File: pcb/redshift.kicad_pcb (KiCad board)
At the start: 4 copper layers, 45 x 63.5 mm, 81 parts, among them IC1 LPC5526JEV98, J1 USB_C_Receptacle_USB2.0, J2 Side, J3 Conn_01x06_Female, J4 Conn_ARM_JTAG_SWD_10, SW1 SW_SP, SW2 SW_SP, SW3 SW_SP, SW4 PTS645, U1 PAW3399DM‐T4QU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

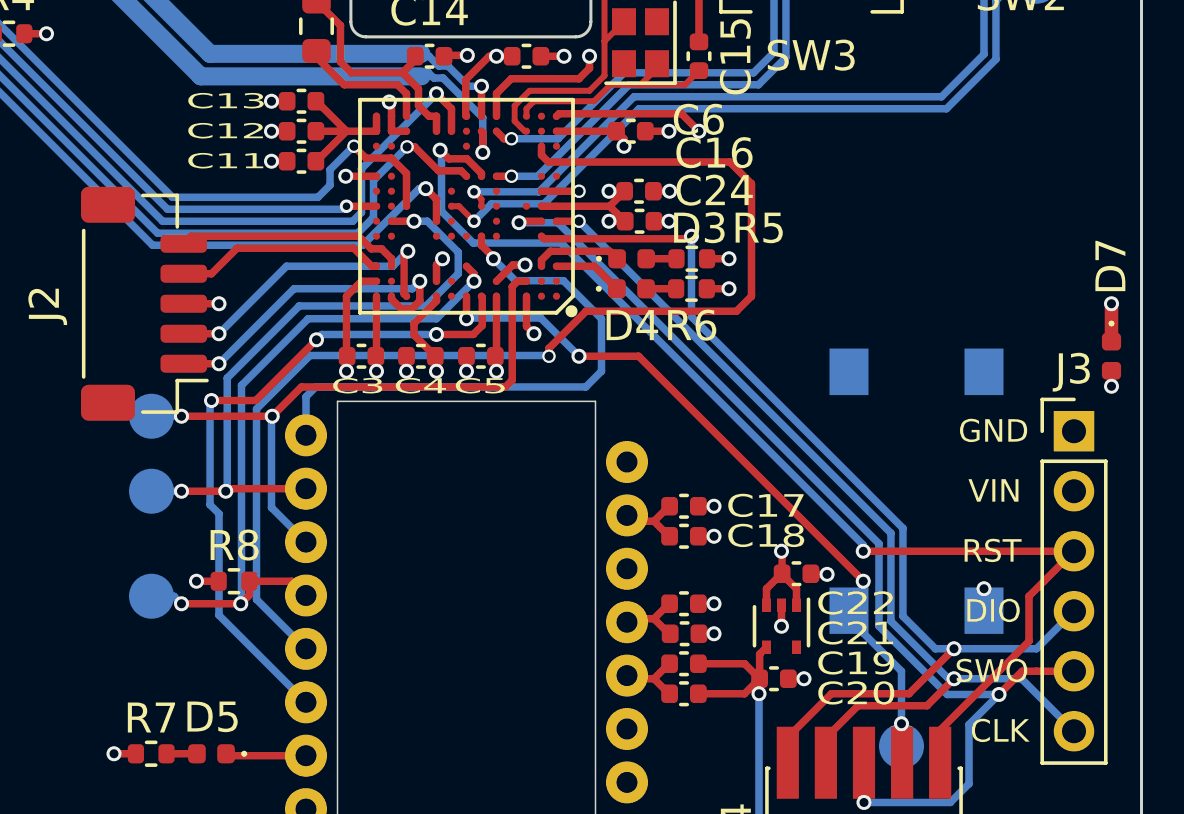
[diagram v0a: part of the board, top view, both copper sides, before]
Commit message: ground unused USB line per datasheet, use smaller switch for ISP
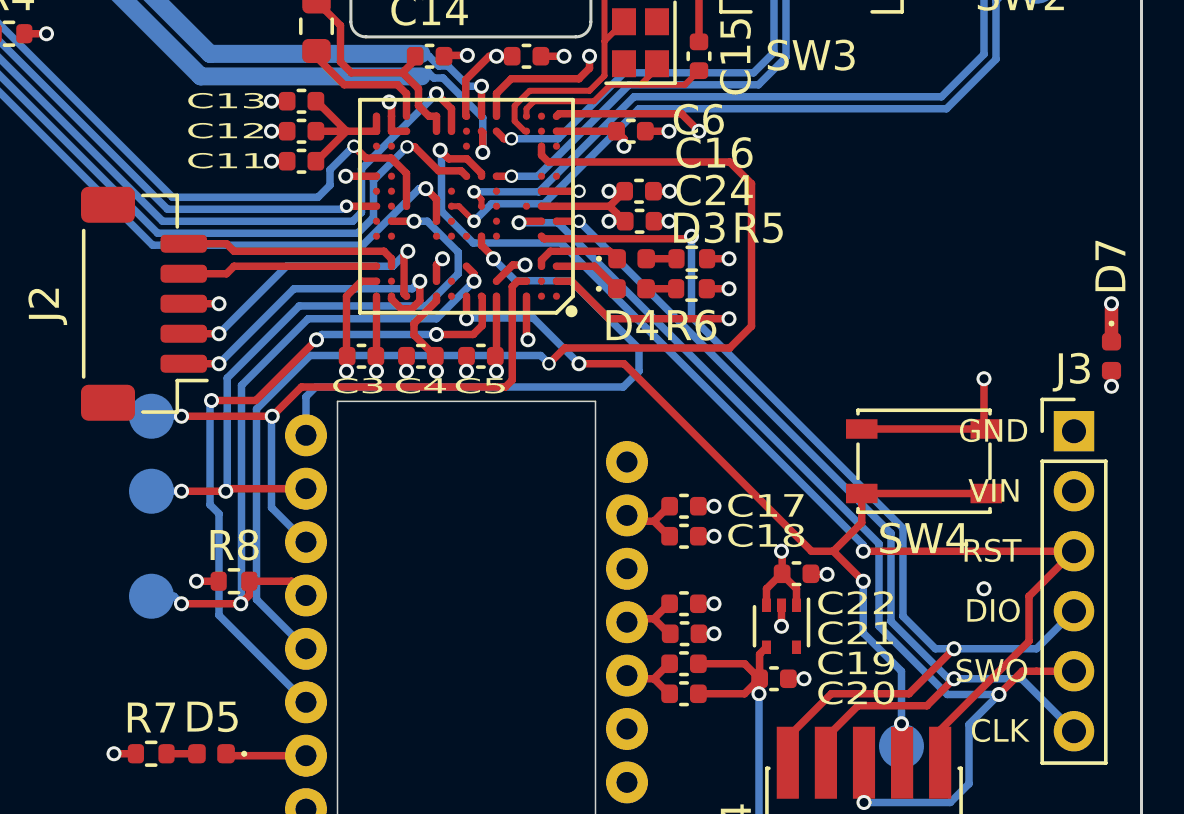
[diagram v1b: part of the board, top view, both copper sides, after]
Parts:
- C11, C14: value 10uF -> 22uF
- C2, C7: value 0.1uF -> 100nF
- SW4: value PTS645 -> PTS810; footprint Button_Switch_SMD:SW_SPST_PTS645 -> Button_Switch_SMD:SW_SPST_PTS810; moved to F.Cu
- moved SW4 1.03 mm to (152.8, 101.5), turned to 180 degrees
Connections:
- IC1 pad B1: unconnected-(IC1-PadB1) -> GND
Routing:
- net GND: track 46.9 -> 59.0 mm, vias 38 -> 40
- net /ISP: track 22.9 -> 29.4 mm
- net /SNSR_MTN: track 18.6 -> 20.5 mm
- net /FC6_CS1: track 38.4 -> 39.0 mm

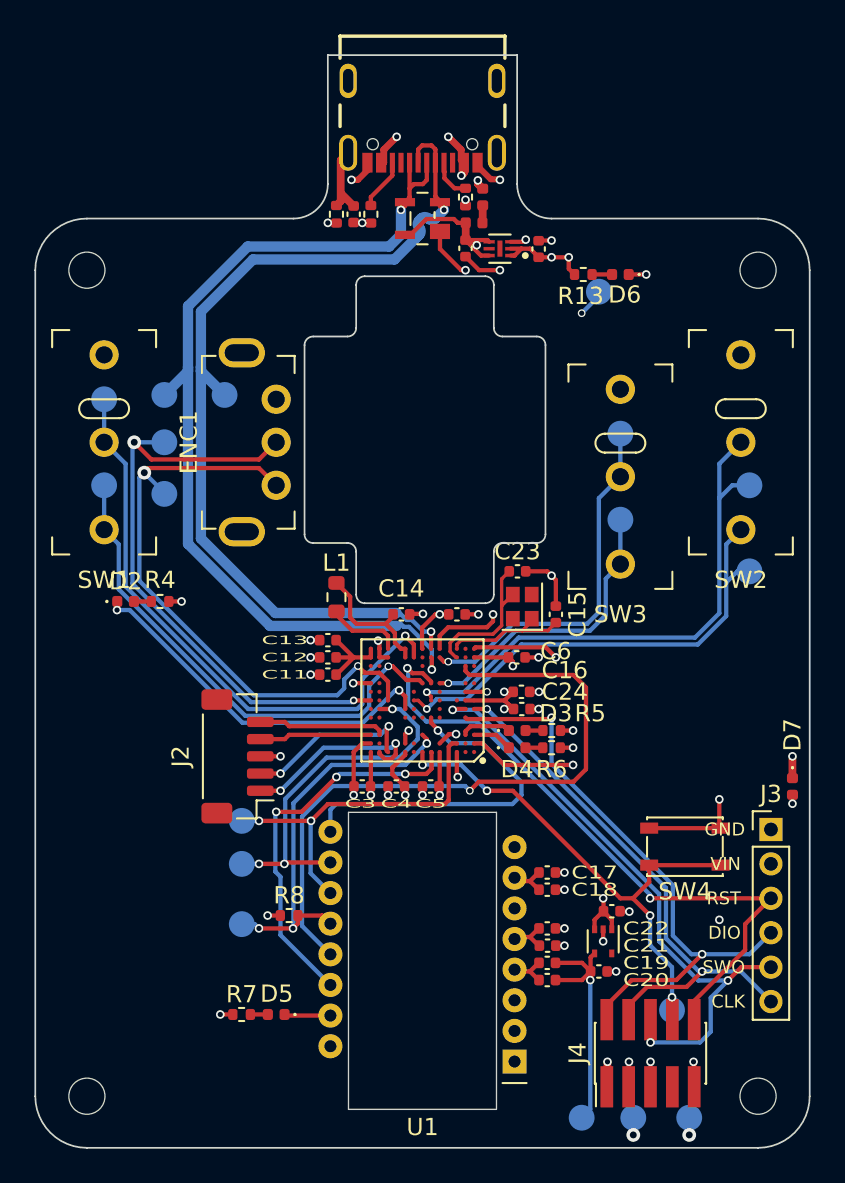
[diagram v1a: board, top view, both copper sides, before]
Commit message: Replaced Old LDO
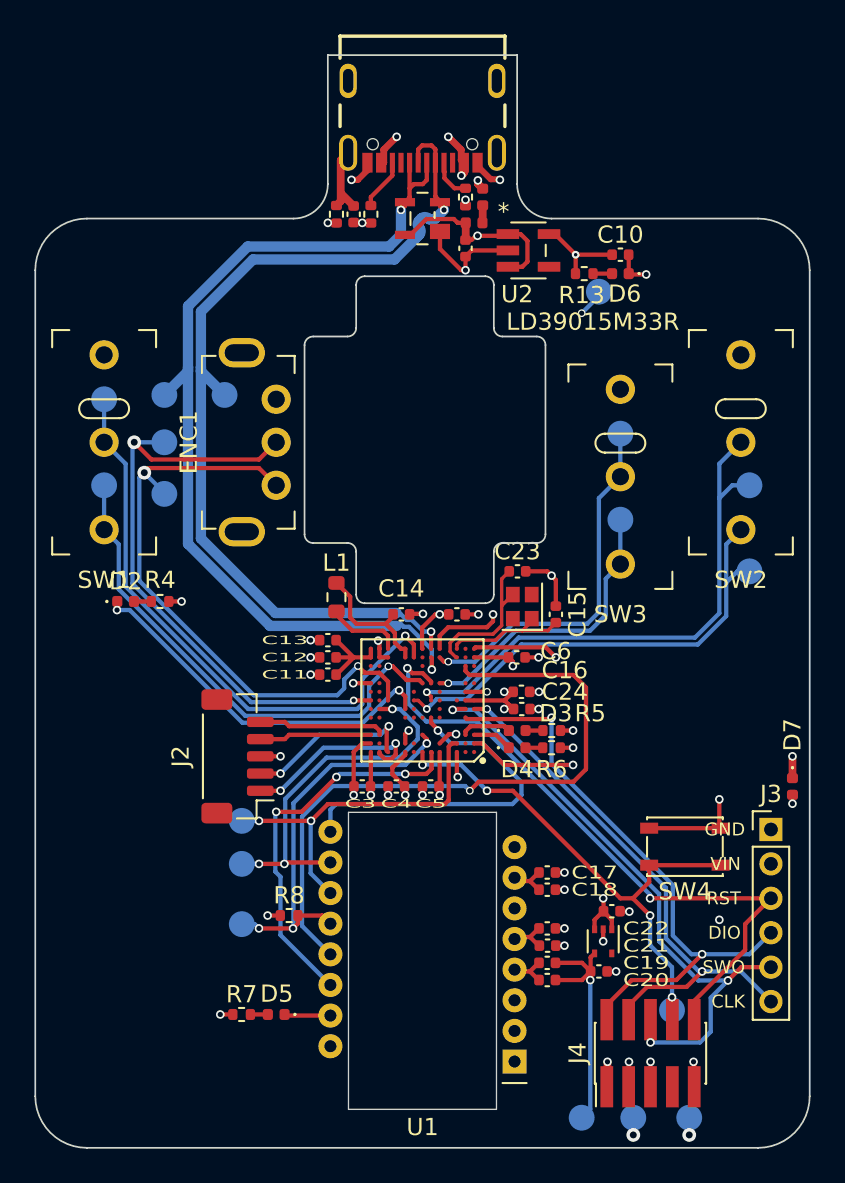
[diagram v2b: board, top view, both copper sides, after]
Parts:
- removed REF** (x4): MountingHole_2.1mm, MountingHole:MountingHole_2.1mm
- removed U4: MIC5528-3.3YMT-TR, MIC5528-3:SON40P120X120X60-7N
- added U2: LD39015M33R, LD39015M33R:LD39015M33R, F.Cu at (143.7, 66.9)
- moved C10 4.76 mm to (149.0, 67.1), turned to 0 degrees
- moved R13 0.07 mm to (146.9, 68.2)
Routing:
- net +5V: track 55.9 -> 58.5 mm
- net GND: track 59.0 -> 59.5 mm, vias 40 -> 37
- net +3V3: track 30.8 -> 30.7 mm, vias 20 -> 19

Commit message: Added cheap and slightly larger 3.3v LDO
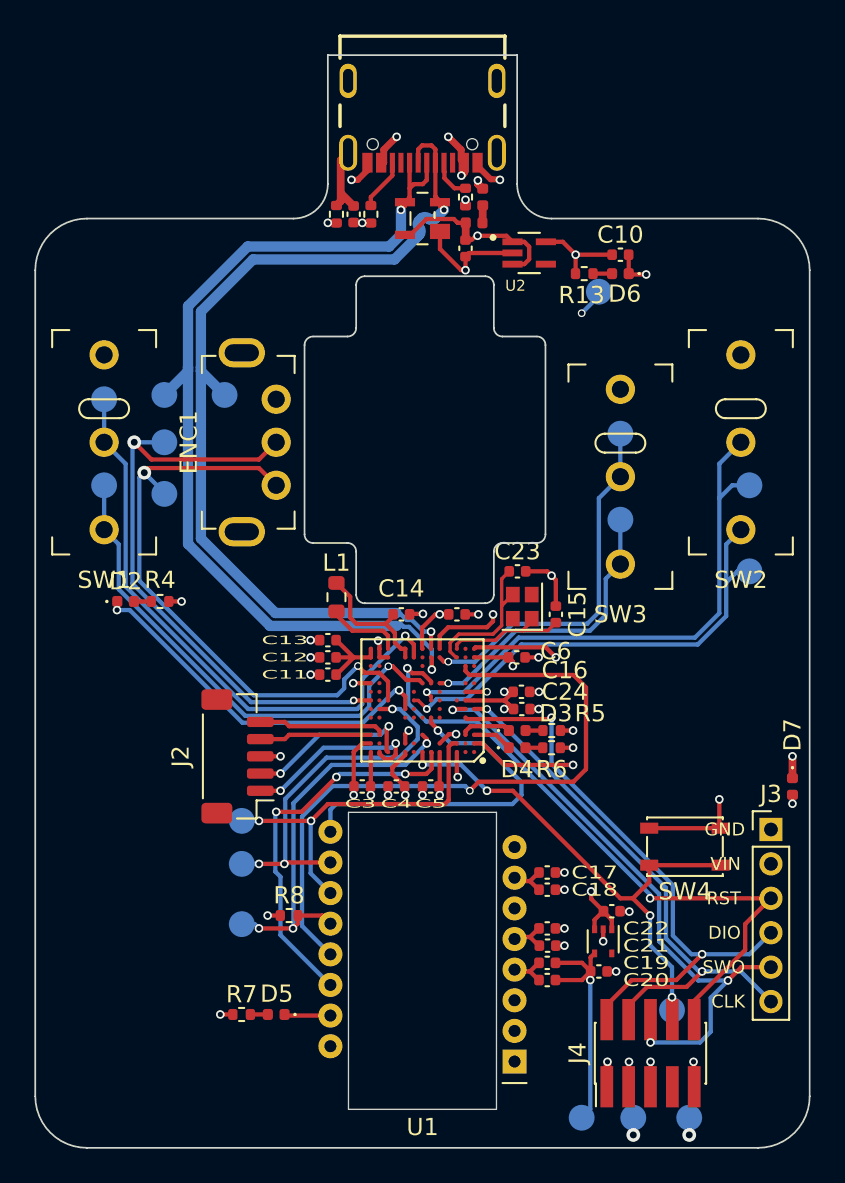
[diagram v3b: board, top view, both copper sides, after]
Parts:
- U2: value LD39015M33R -> MIC5365-3.3YC5-TR; footprint LD39015M33R:LD39015M33R -> MIC5365-3.3YC5-TR:SOT65P210X110-5N
- moved U2 0.15 mm to (143.7, 67.0)
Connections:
- U2 pad 4: unconnected-(U2-Pad4) -> (no net)
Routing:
- net GND: track 59.5 -> 59.7 mm, vias 37 -> 36

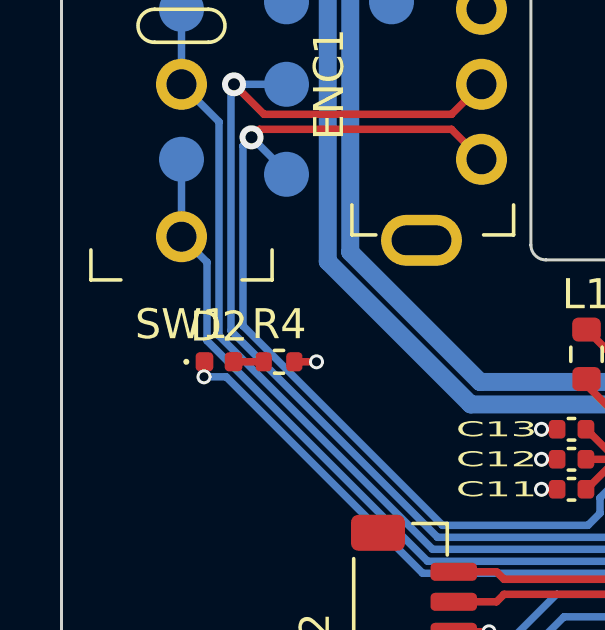
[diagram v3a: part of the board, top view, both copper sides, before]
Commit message: Added the only missing lib I could find: the mcu
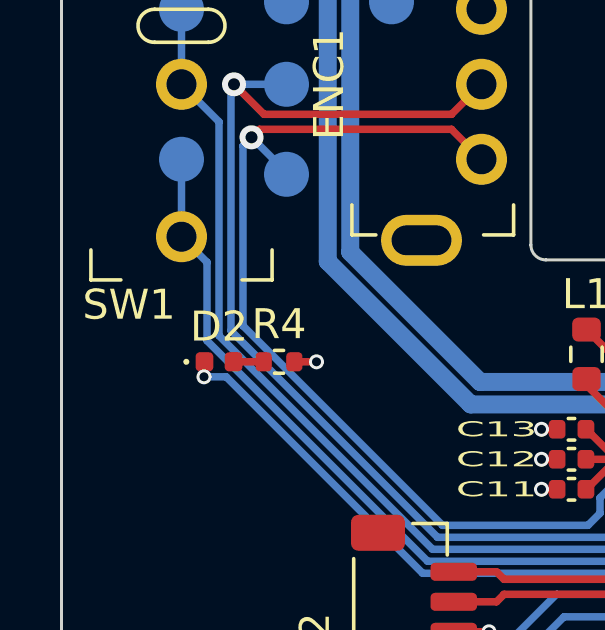
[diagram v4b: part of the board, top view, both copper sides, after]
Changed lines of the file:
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@@
     (property "Sheetname" "")
     (attr through_hole)
-    (fp_text reference "SW1" (at 8 0) (layer "F.SilkS")
+    (fp_text reference "SW1" (at 7.35 1.75) (layer "F.SilkS")
       (effects (font (size 1 1) (thickness 0.15)))
     )

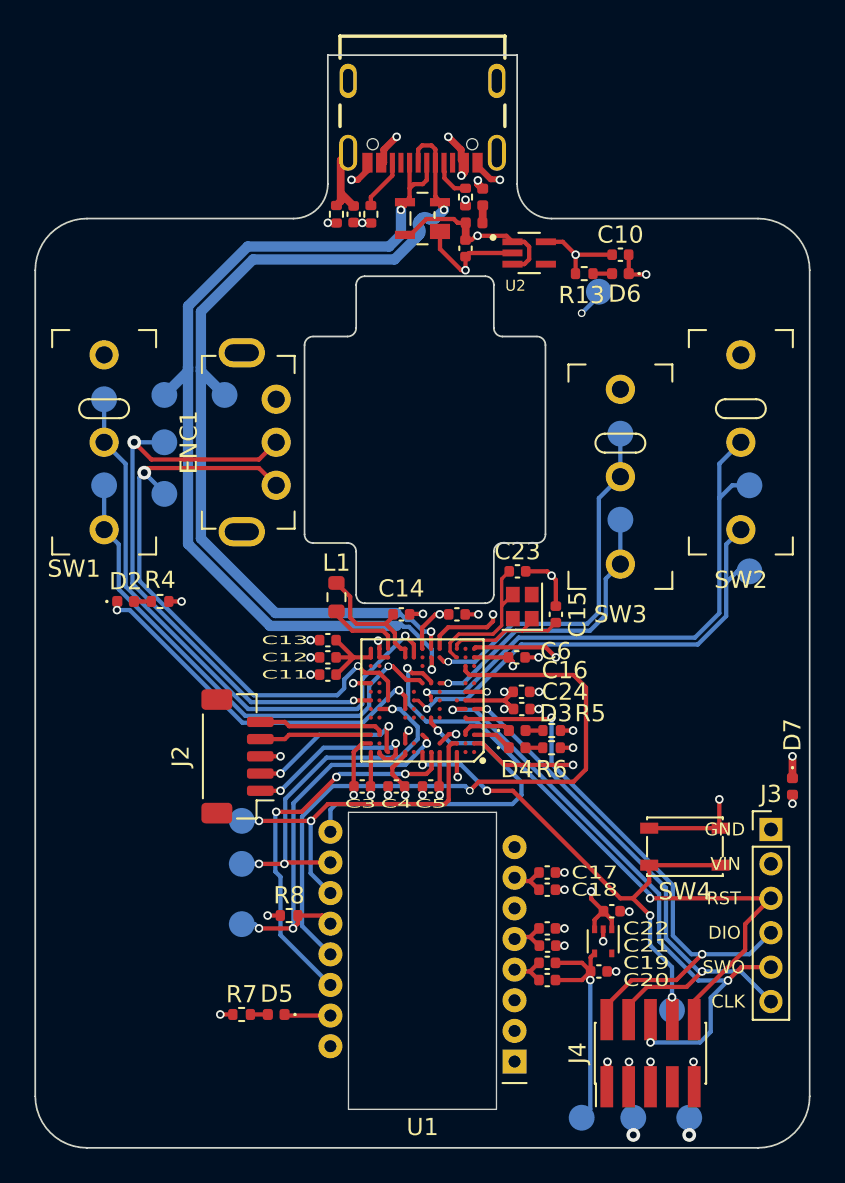
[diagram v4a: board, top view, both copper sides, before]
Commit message: Modified PCB to reflect changes Moved some silkscreens and parts around to fit better Changed default VIA size to match what's being used
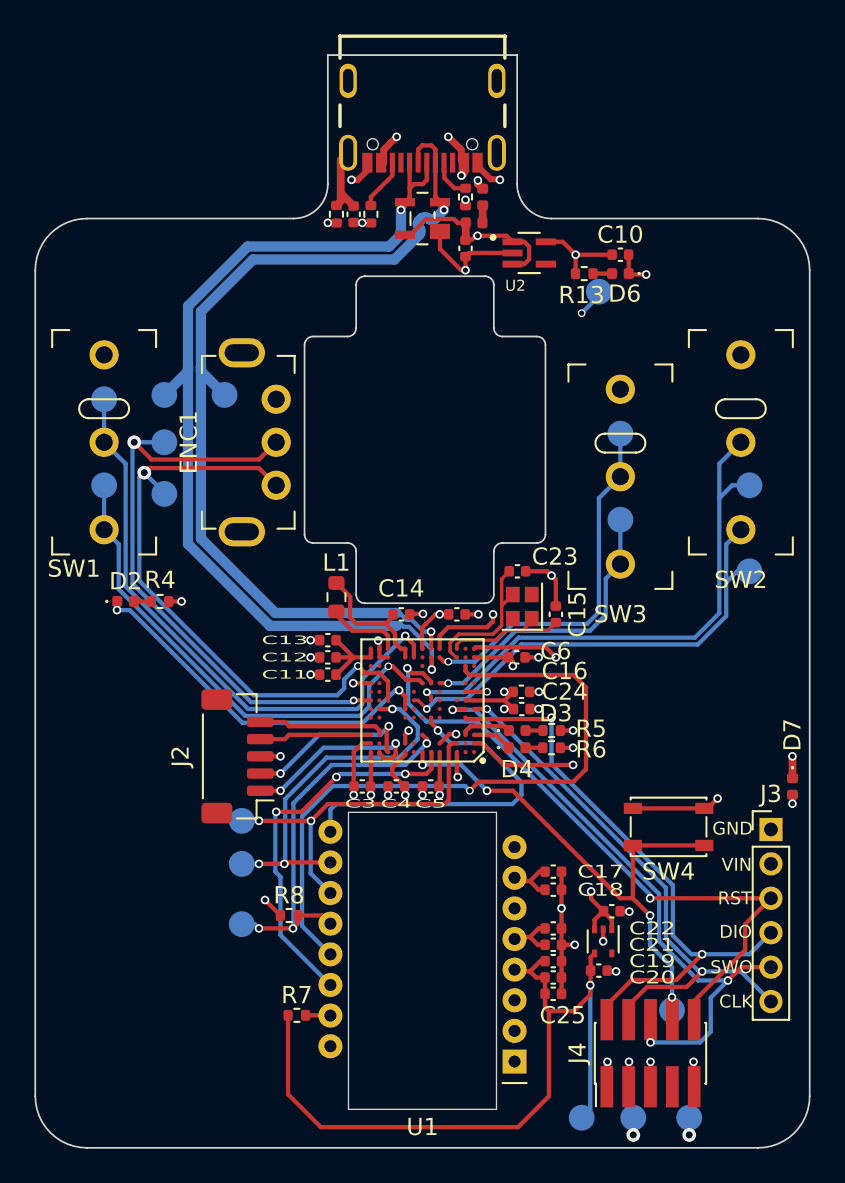
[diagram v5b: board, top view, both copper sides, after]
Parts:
- removed D5: RED, LED_SMD:LED_0402_1005Metric
- added C25: 22uF, Capacitor_SMD:C_0402_1005Metric, F.Cu at (145.1, 110.0)
- R7: value 10k -> 9.31+-1%
- moved R7 3.21 mm to (130.2, 111.3)
- moved SW4 1.49 mm to (151.8, 100.3)
- moved C20 0.38 mm to (145.1, 109.1)
- moved C19 0.36 mm to (145.1, 108.2)
- moved C17 0.35 mm to (145.1, 103.0)
- moved C18 0.35 mm to (145.1, 104.0)
- moved C22 0.35 mm to (145.1, 106.2)
- moved C21 0.33 mm to (145.1, 107.2)
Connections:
- C17 pad 1: +3V3 -> GND
- C17 pad 2: Net-(C17-Pad2) -> +3V3
- C18 pad 1: +3V3 -> GND
- C18 pad 2: Net-(C17-Pad2) -> +3V3
- C19 pad 1: Net-(C19-Pad1) -> +1V8
- C19 pad 2: +1V8 -> GND
- C20 pad 1: Net-(C19-Pad1) -> +1V8
- C20 pad 2: +1V8 -> GND
- R7 pad 1: +3V3 -> +1V8
- R7 pad 2: Net-(D5-Pad2) -> Net-(U1-Pad15)
- R8 pad 1: GND -> +3V3
- U1 pad 15: /SNSR_LED -> Net-(U1-Pad15)
- U1 pad 4: Net-(C19-Pad1) -> +1V8
- U1 pad 7: Net-(C17-Pad2) -> +3V3
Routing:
- net +1V8: track 14.4 -> 44.6 mm
- net +3V3: track 30.6 -> 43.1 mm, vias 19 -> 17
- net GND: track 59.7 -> 66.2 mm, vias 36 -> 35
- net /SNSR_LED: track 2.69 -> 0.00 mm
- net Net-(C17-Pad2): track 2.43 -> 0.00 mm
- net Net-(C19-Pad1): track 2.40 -> 0.00 mm
- net Net-(U1-Pad15): track 0.00 -> 1.45 mm
- net Net-(D5-Pad2): track 1.01 -> 0.00 mm
- net /ISP: track 29.4 -> 30.1 mm
- net Net-(C21-Pad1): track 2.42 -> 3.08 mm
